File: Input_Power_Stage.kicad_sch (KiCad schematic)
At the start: 25 parts, among them Q1 MMBT3904, Q2 MMBT3904, Q3 MMBT3904, U1 TPS2121RUXR, U2 AP2112K-3.3, U3 TLV431

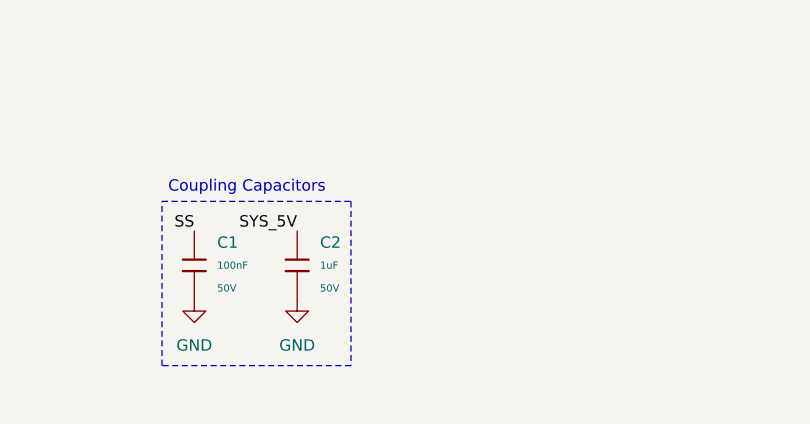
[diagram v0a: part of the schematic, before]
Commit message: Finished USB programming stage
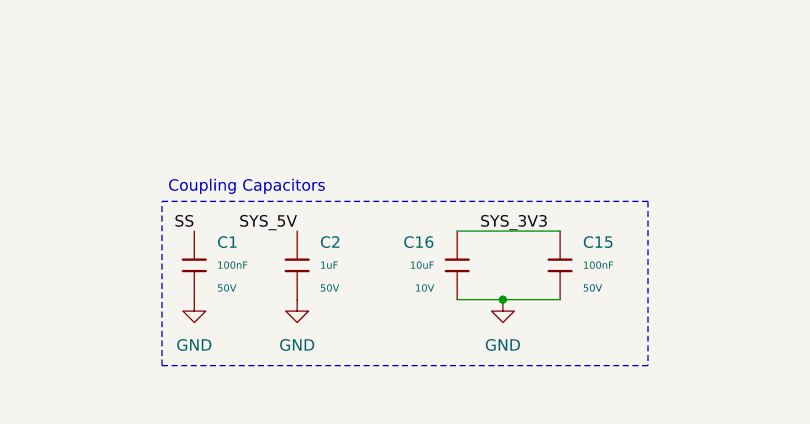
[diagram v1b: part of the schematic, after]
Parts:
- added C15: 100nF, PCM_JLCPCB:C_0603, symbol PCM_JLCPCB-Capacitors:0603,100nF
- added C16: 10uF, PCM_JLCPCB:C_0603, symbol PCM_JLCPCB-Capacitors:0603,10uF
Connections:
- net GND: now also C15.1, C16.2
- net SYS_3V3: now also C15.2, C16.1

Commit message: Finished STM32 Stage
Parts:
- renumbered C16 to C3, C15 to C4, C3 to C5, R7 to R10, R6 to R11, R9 to R12, R8 to R13, R12 to R14, R10 to R15, R15 to R16, R14 to R17, R3 to R6, R4 to R7, R13 to R8, R11 to R9, U1 to U2, U2 to U3, U3 to U4

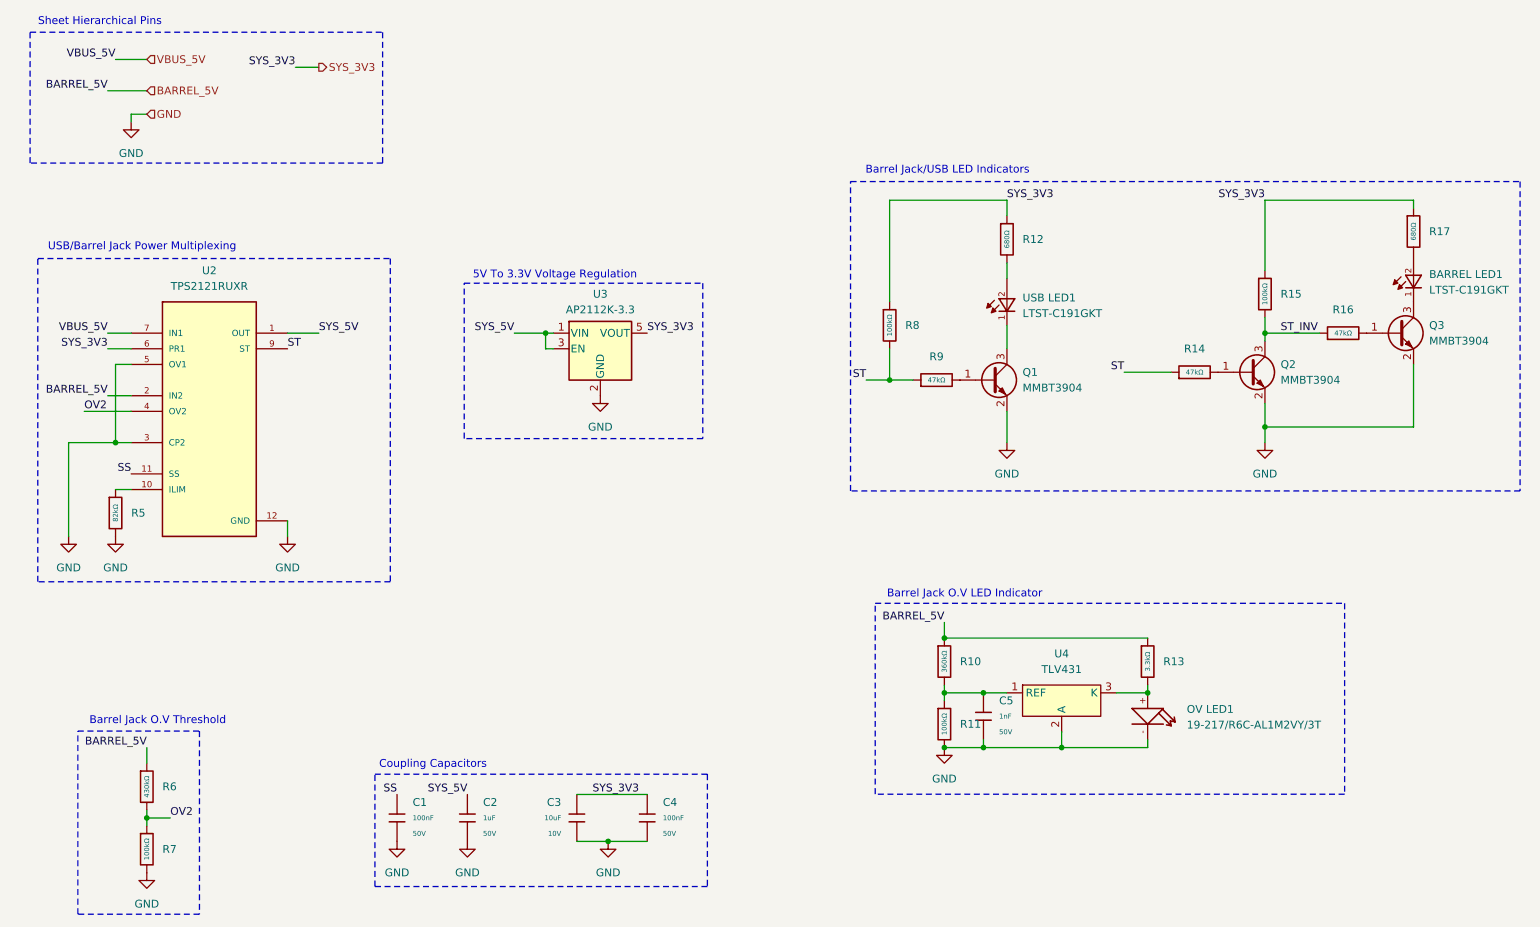
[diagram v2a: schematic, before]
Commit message: - Added Hysteresis resistor on TLV431BSN1T1G - Lowered TLV431BSN1T1G impedance values for resistors on the voltage divider
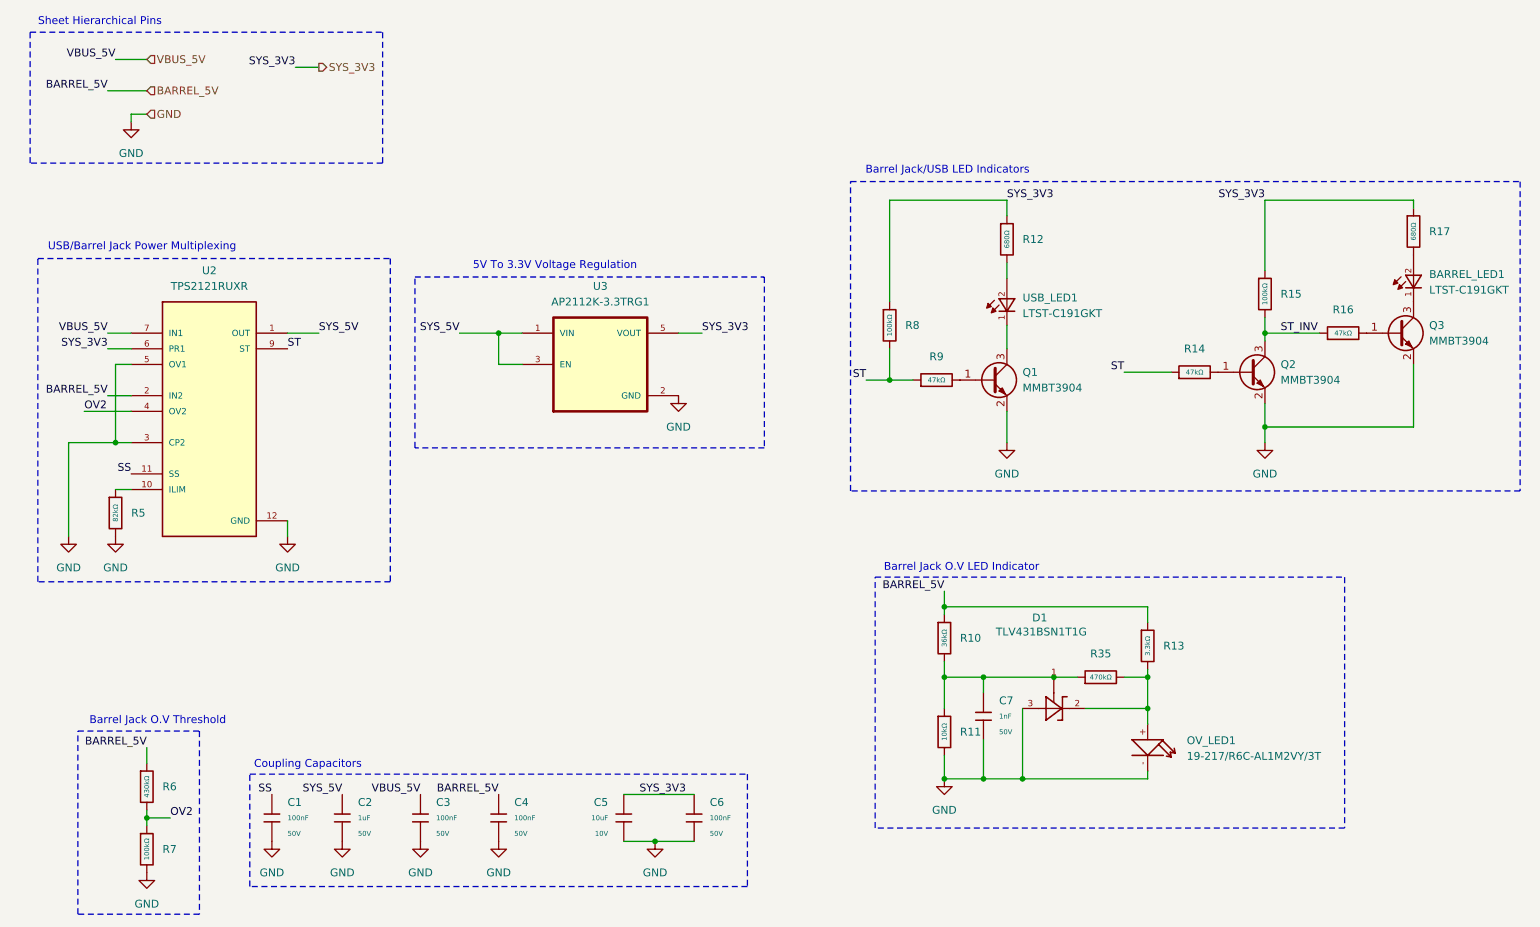
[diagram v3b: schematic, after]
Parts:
- removed R10: 360kΩ, PCM_JLCPCB:R_0603, symbol PCM_JLCPCB-Resistors:0603,360kΩ
- removed R11: 100kΩ, PCM_JLCPCB:R_0603, symbol PCM_JLCPCB-Resistors:0603,100kΩ
- removed U3: AP2112K-3.3, Package_TO_SOT_SMD:SOT-23-5, symbol Regulator_Linear:AP2112K-3.3
- removed U4: TLV431, symbol TLV431QFTA:TLV431QFTA
- added C3, C4: 100nF, PCM_JLCPCB:C_0603, symbol PCM_JLCPCB-Capacitors:0603,100nF
- added D1: TLV431BSN1T1G, TLV431 - Voltage Ref:SOT23, symbol TLV431BSN1T1G:TLV431BSN1T1G
- added R10: 36kΩ, PCM_JLCPCB:R_0603, symbol PCM_JLCPCB-Resistors:0603,36kΩ
- added R11: 10kΩ, PCM_JLCPCB:R_0603, symbol PCM_JLCPCB-Resistors:0603,10kΩ
- added R35: 470kΩ, PCM_JLCPCB:R_0603, symbol PCM_JLCPCB-Resistors:0603,470kΩ
- added U3: AP2112K-3.3TRG1, Voltage DV - AP2112K3.3:SOT95P285X140-5N, symbol AP2112K-3.3TRG1:AP2112K-3.3TRG1
- BARREL_LED1: renamed from BARREL LED1; footprint LTST-C191GKT:0603 -> GREEN LED Indicator - LTST-C191GKT:0603
- OV_LED1: renamed from OV LED1; footprint LED-SMD-RED-DIFFUSED_0603_:LED-0603 -> RED LED Indicator - LED-SMD-RED-DIFFUSED_0603:LED-0603
- U2: footprint TPS2121RUXR:IC_TPS2121RUXR -> Power Muxer - TPS2121RUXR:IC_TPS2121RUXR
- USB_LED1: renamed from USB LED1; footprint LTST-C191GKT:0603 -> GREEN LED Indicator - LTST-C191GKT:0603
- renumbered C3 to C5, C4 to C6, C5 to C7
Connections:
- net BARREL_5V: now also C4.1, R10.1
- net GND: now also C3.2, C4.2, D1.3, R11.2, U3.2 (GND)
- net SYS_3V3: now also U3.5 (VOUT)
- net SYS_5V: now also U3.1 (VIN), U3.3 (EN)
- net VBUS_5V: now also C3.1
- net at C7.1: now also D1.1, R10.2, R11.1, R35.1
- net at OV_LED1.+, R13.2: now also D1.2, R35.2
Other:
- company: Yaniv Lieberman -> (none)
- moved on the sheet: C1, C2, C5, C6, OV_LED1, R13
